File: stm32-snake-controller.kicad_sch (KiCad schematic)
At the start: 46 parts, among them J101 Barrel_Jack_MountingPin, J101 Tag Connector, J102 USB_A, J103 JST 2.54 Header, Q101 AO3501A, SW106 SW_Push, U101 STM32F401RCTx, U102 USBLC6-2SC6, U104 M24C64-RMN, Y101 16MHz, Y103 32.768kHz

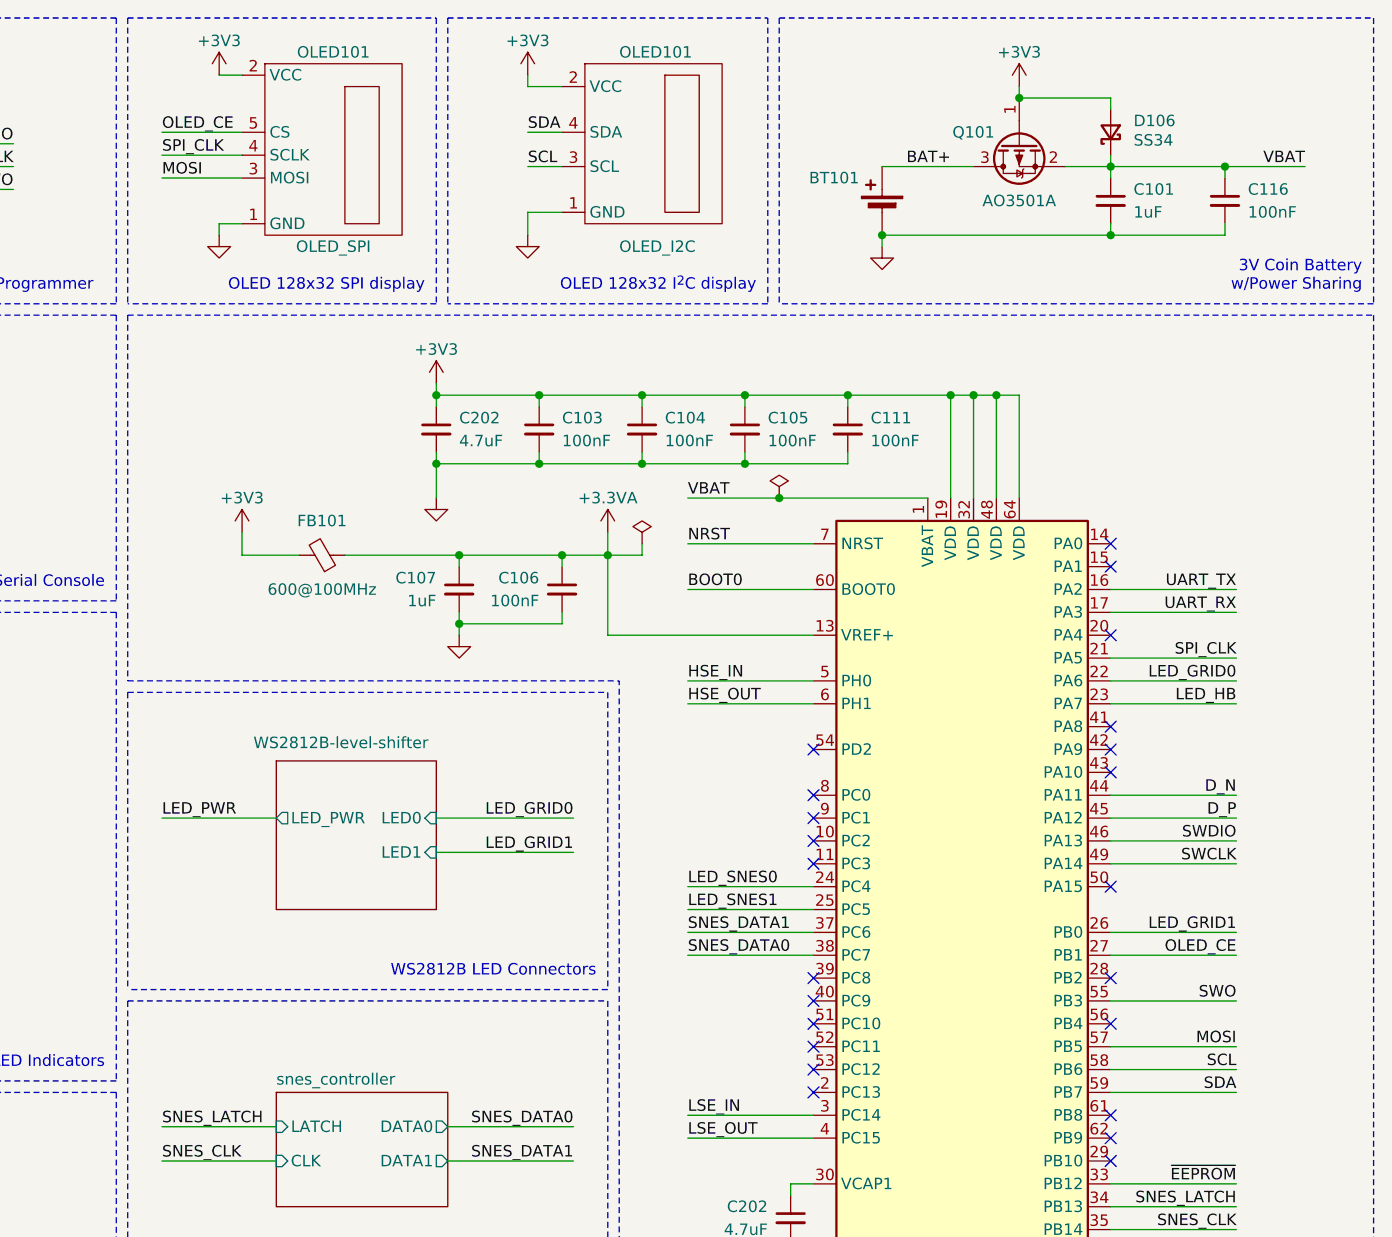
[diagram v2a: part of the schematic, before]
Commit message: update SPI pins for OLED
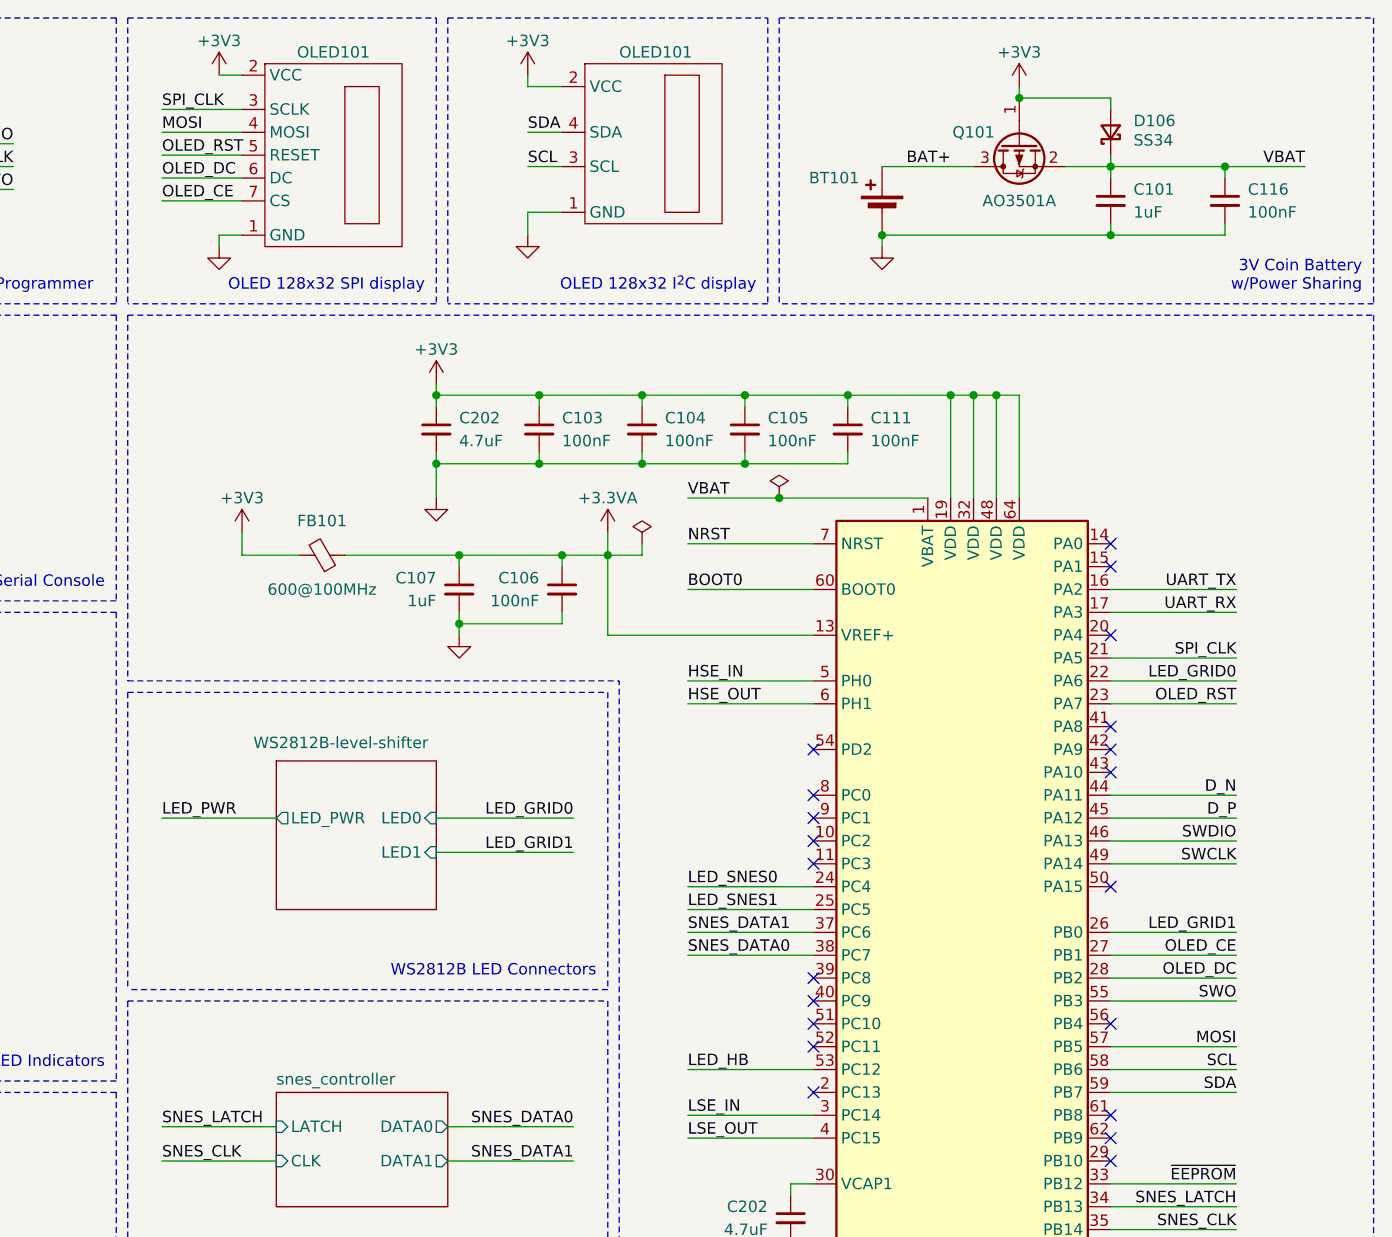
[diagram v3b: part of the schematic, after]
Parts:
- OLED101: footprint Connector_JST:JST_XH_B5B-XH-A_1x05_P2.50mm_Vertical -> Connector_JST:JST_XH_B7B-XH-A_1x07_P2.50mm_Vertical
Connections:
- net LED_HB: now also U101.53 (PC12); no longer U101.23 (PA7)
- net MOSI: now also OLED101.4 (MOSI); no longer OLED101.3 (MOSI)
- net OLED_CE: now also OLED101.7 (CS); no longer OLED101.5 (CS)
- net SPI_CLK: now also OLED101.3 (SCLK); no longer OLED101.4 (SCLK)
- net OLED_DC: now reaches U101.28 (PB2)
- net OLED_DC: now also OLED101.6 (DC)
- new net OLED_RST: OLED101.5 (RESET), U101.23 (PA7)
- no-connect marks 25 -> 23
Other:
- company: (none) -> Butler Electronics
- title: (none) -> STM32 Snake Game Control Board
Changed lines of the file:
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@@
 (kicad_sch (version 20230121) (generator eeschema)
   (paper "A4")
+  (title_block
+    (title "STM32 Snake Game Control Board")
+    (date "2024-01-01")
+    (rev "A")
+    (company "Butler Electronics")
+    (comment 1 "Joshua Butler, MD, MHI")
+  )
   (junction (at 60.96 81.28) (diameter 0) (color 0 0 0 0)
   )
@@
   (no_connect (at 220.98 128.27))
   (no_connect (at 254 95.25))
-  (no_connect (at 220.98 130.81))
   (no_connect (at 220.98 133.35))
   (no_connect (at 220.98 105.41))
-  (no_connect (at 254 120.65))
   (no_connect (at 110.49 27.94))
   (no_connect (at 254 92.71))
@@
     (stroke (width 0) (type default))
   )
+  (wire (pts (xy 148.59 34.29) (xy 157.48 34.29))
+    (stroke (width 0) (type default))
+  )
   (polyline (pts (xy 144.78 13.97) (xy 179.07 13.97))
     (stroke (width 0) (type dash))
@@
     (stroke (width 0) (type default))
   )
-  (wire (pts (xy 154.94 36.83) (xy 154.94 38.1))
+  (wire (pts (xy 154.94 38.1) (xy 154.94 39.37))
     (stroke (width 0) (type default))
   )
@@
     (stroke (width 0) (type default))
   )
+  (wire (pts (xy 254 120.65) (xy 267.97 120.65))
+    (stroke (width 0) (type default))
+  )
   (wire (pts (xy 148.59 102.87) (xy 161.29 102.87))
     (stroke (width 0) (type default))
@@
     (stroke (width 0) (type dash))
   )
+  (wire (pts (xy 207.01 130.81) (xy 220.98 130.81))
+    (stroke (width 0) (type default))
+  )
   (wire (pts (xy 80.01 21.59) (xy 80.01 24.13))
     (stroke (width 0) (type default))
@@
     (stroke (width 0) (type default))
   )
+  (wire (pts (xy 148.59 24.13) (xy 157.48 24.13))
+    (stroke (width 0) (type default))
+  )
   (wire (pts (xy 60.96 78.74) (xy 62.23 78.74))
     (stroke (width 0) (type default))
@@
     (stroke (width 0) (type default))
   )
-  (wire (pts (xy 157.48 36.83) (xy 154.94 36.83))
+  (wire (pts (xy 157.48 38.1) (xy 154.94 38.1))
     (stroke (width 0) (type default))
   )
@@
     (effects (font (size 1.27 1.27)) (justify right bottom))
   )
-  (label "OLED_CE" (at 148.59 26.67 0) (fields_autoplaced)
+  (label "OLED_CE" (at 148.59 34.29 0) (fields_autoplaced)
     (effects (font (size 1.27 1.27)) (justify left bottom))
   )
@@
     (effects (font (size 1.27 1.27)) (justify left bottom))
   )
+  (label "OLED_RST" (at 267.97 90.17 180) (fields_autoplaced)
+    (effects (font (size 1.27 1.27)) (justify right bottom))
+  )
   (label "UART_TX" (at 128.27 62.23 180) (fields_autoplaced)
     (effects (font (size 1.27 1.27)) (justify right bottom))
@@
     (effects (font (size 1.27 1.27)) (justify right bottom))
   )
+  (label "OLED_DC" (at 148.59 31.75 0) (fields_autoplaced)
+    (effects (font (size 1.27 1.27)) (justify left bottom))
+  )
   (label "D_P" (at 267.97 102.87 180) (fields_autoplaced)
     (effects (font (size 1.27 1.27)) (justify right bottom))
@@
     (effects (font (size 1.27 1.27)) (justify left bottom))
   )
+  (label "OLED_RST" (at 148.59 29.21 0) (fields_autoplaced)
+    (effects (font (size 1.27 1.27)) (justify left bottom))
+  )
   (label "SNES_DATA1" (at 207.01 115.57 0) (fields_autoplaced)
     (effects (font (size 1.27 1.27)) (justify left bottom))
@@
     (effects (font (size 1.27 1.27)) (justify left bottom))
   )
+  (label "OLED_DC" (at 267.97 120.65 180) (fields_autoplaced)
+    (effects (font (size 1.27 1.27)) (justify right bottom))
+  )
   (label "HSE_IN" (at 207.01 87.63 0) (fields_autoplaced)
     (effects (font (size 1.27 1.27)) (justify left bottom))
@@
     (effects (font (size 1.27 1.27)) (justify right bottom))
   )
-  (label "SPI_CLK" (at 148.59 29.21 0) (fields_autoplaced)
+  (label "SPI_CLK" (at 148.59 24.13 0) (fields_autoplaced)
     (effects (font (size 1.27 1.27)) (justify left bottom))
   )
@@
     (effects (font (size 1.27 1.27)) (justify right bottom))
   )
-  (label "MOSI" (at 148.59 31.75 0) (fields_autoplaced)
+  (label "MOSI" (at 148.59 26.67 0) (fields_autoplaced)
     (effects (font (size 1.27 1.27)) (justify left bottom))
   )
@@
     (effects (font (size 1.27 1.27)) (justify right bottom))
   )
-  (label "LED_HB" (at 267.97 90.17 180) (fields_autoplaced)
-    (effects (font (size 1.27 1.27)) (justify right bottom))
+  (label "LED_HB" (at 207.01 130.81 0) (fields_autoplaced)
+    (effects (font (size 1.27 1.27)) (justify left bottom))
   )
   (symbol (lib_id "power:GND") (at 127 125.73 0) (unit 1)
@@
     )
   )
-  (symbol (lib_id "power:GND") (at 154.94 38.1 0) (unit 1)
+  (symbol (lib_id "power:GND") (at 154.94 39.37 0) (unit 1)
     (in_bom yes) (on_board yes) (dnp no) (fields_autoplaced)
-    (property "Reference" "#PWR010" (at 154.94 44.45 0)
-      (effects (font (size 1.27 1.27)) hide)
-    )
-    (property "Value" "GND" (at 154.94 43.18 0)
-      (effects (font (size 1.27 1.27)) hide)
-    )
-    (property "Footprint" "" (at 154.94 38.1 0)
-      (effects (font (size 1.27 1.27)) hide)
-    )
-    (property "Datasheet" "" (at 154.94 38.1 0)
+    (property "Reference" "#PWR010" (at 154.94 45.72 0)
+      (effects (font (size 1.27 1.27)) hide)
+    )
+    (property "Value" "GND" (at 154.94 44.45 0)
+      (effects (font (size 1.27 1.27)) hide)
+    )
+    (property "Footprint" "" (at 154.94 39.37 0)
+      (effects (font (size 1.27 1.27)) hide)
+    )
+    (property "Datasheet" "" (at 154.94 39.37 0)
       (effects (font (size 1.27 1.27)) hide)
     )
@@
     )
     (property "Value" "OLED_I2C" (at 199.39 39.37 0)
-      (effects (font (size 1.27 1.27)) (justify left))
+      (effects (font (size 1.27 1.27)) (justify left) hide)
     )
     (property "Footprint" "Connector_JST:JST_XH_B4B-XH-A_1x04_P2.50mm_Vertical" (at 203.2 39.37 0)
@@
       (effects (font (size 1.27 1.27)))
     )
-    (property "Value" "OLED_SPI" (at 167.64 39.37 0)
-      (effects (font (size 1.27 1.27)))
-    )
-    (property "Footprint" "Connector_JST:JST_XH_B5B-XH-A_1x05_P2.50mm_Vertical" (at 167.64 40.64 0)
+    (property "Value" "OLED_SPI" (at 167.64 40.64 0)
+      (effects (font (size 1.27 1.27)) hide)
+    )
+    (property "Footprint" "Connector_JST:JST_XH_B7B-XH-A_1x07_P2.50mm_Vertical" (at 167.64 40.64 0)
       (effects (font (size 1.27 1.27)) hide)
     )
     (property "Datasheet" "" (at 167.64 29.21 0)
+      (effects (font (size 1.27 1.27)) hide)
+    )
+    (property "LCSC" "" (at 167.64 29.21 0)
+      (effects (font (size 1.27 1.27)) hide)
+    )
+    (property "Mouser" "" (at 167.64 29.21 0)
       (effects (font (size 1.27 1.27)) hide)
     )
@@
     (pin "4")
     (pin "2")
-    (instances
-      (project "stm32-snake-controller"
+    (pin "7")
+    (pin "6")
+    (instances
+      (project "stm32-snake-controller"

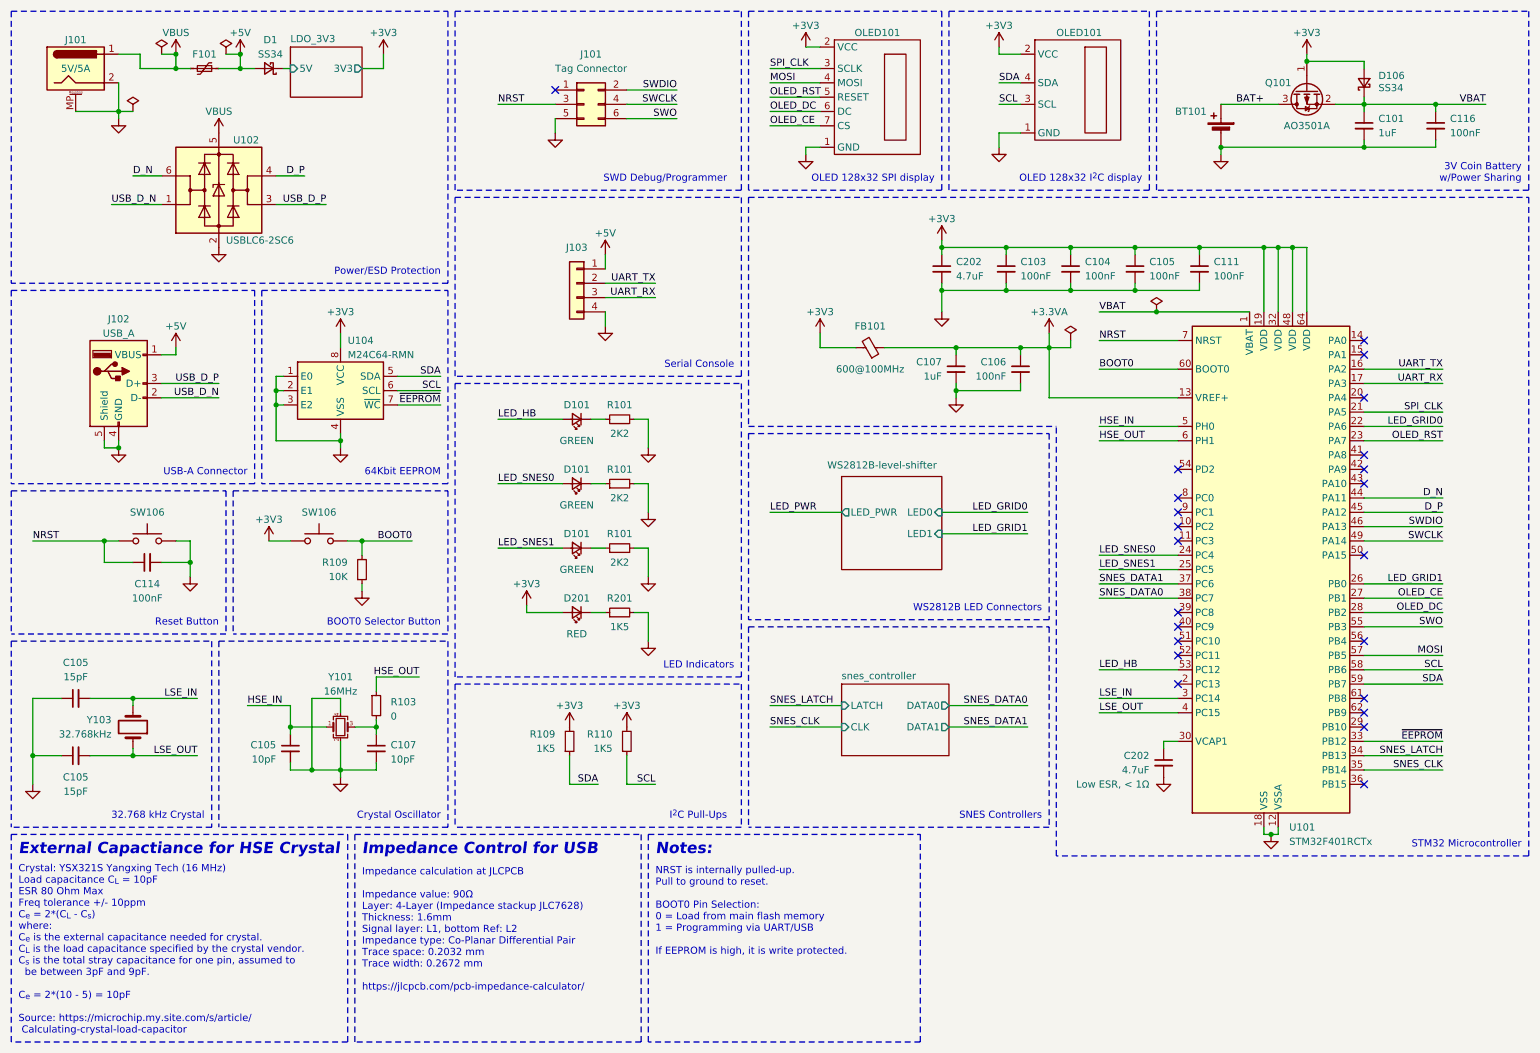
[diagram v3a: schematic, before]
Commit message: add power switch for USB Host
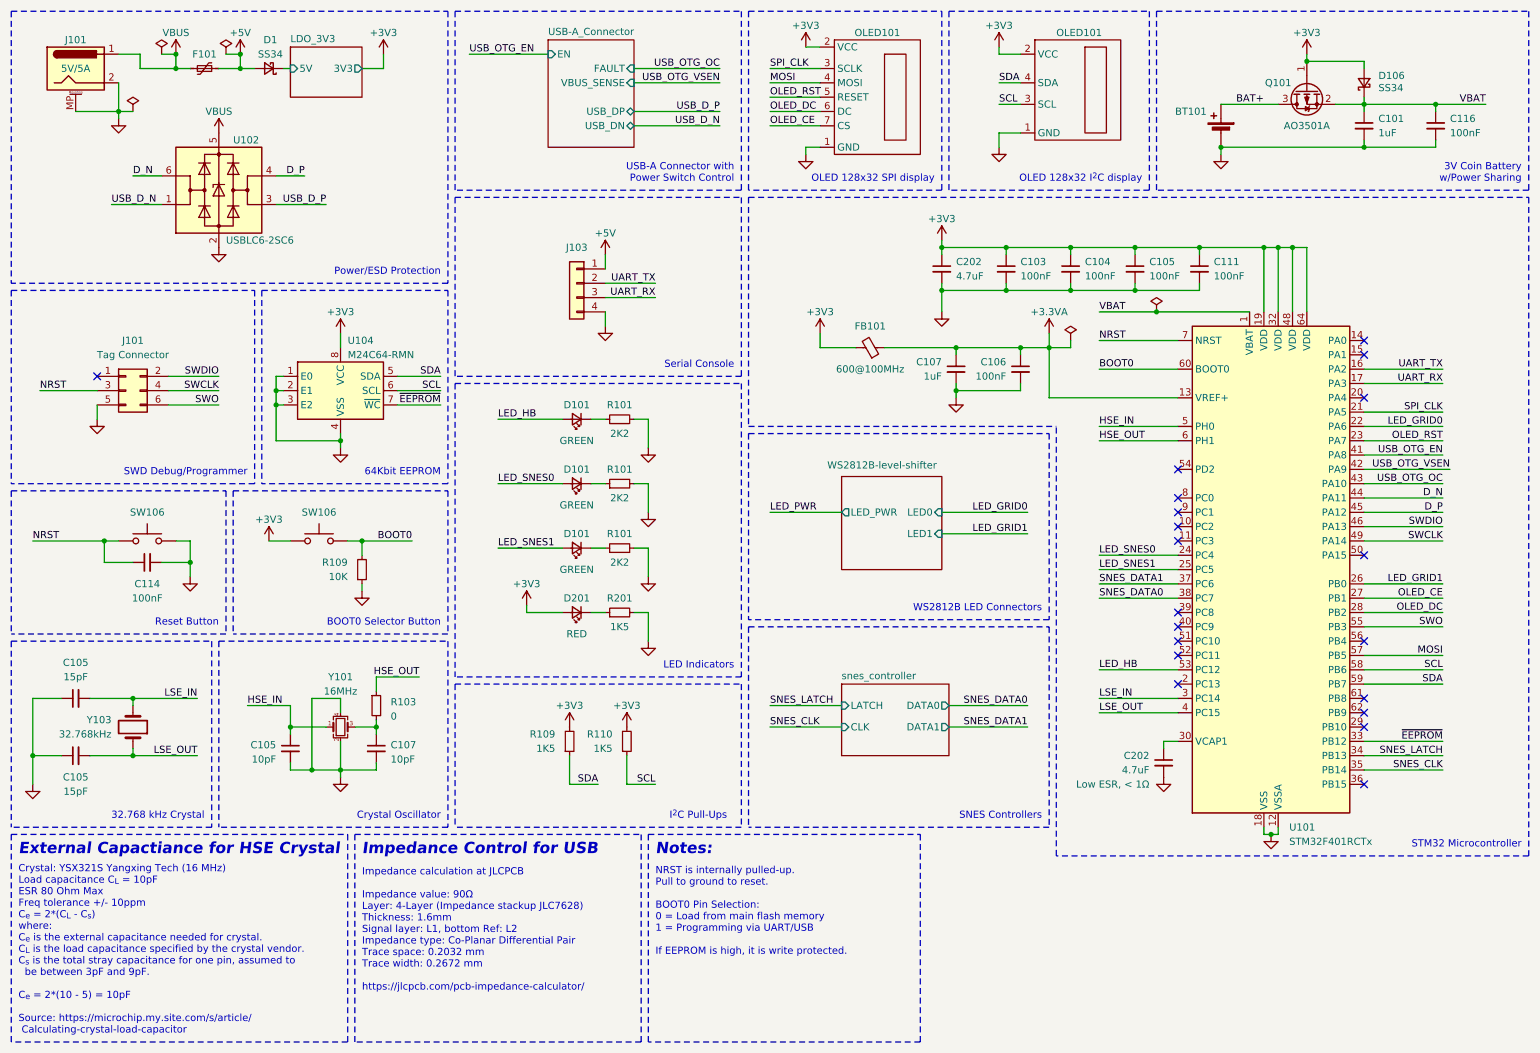
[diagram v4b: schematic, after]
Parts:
- removed J102: USB_A, Connector_USB:USB_A_CONNFLY_DS1095-WNR0, symbol Connector:USB_A
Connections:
- net USB_OTG_EN: now reaches U101.41 (PA8)
- net USB_OTG_VSEN: now reaches U101.42 (PA9)
- net USB_OTG_OC: now reaches U101.43 (PA10)
- no-connect marks 23 -> 20
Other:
- added sheet USB-A_Connector (USB-A_connector.kicad_sch)
- note added: "USB-A Connector with Power Switch Control"
- note removed: "USB-A Connector"
- moved on the sheet: J101
